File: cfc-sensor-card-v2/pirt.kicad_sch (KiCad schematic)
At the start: 82 parts, among them Q6 PMV45EN, Q7 DMP3050LVT-7, U1 TLC3704, U10 LT3042IMSE, U11 LT3042IMSE, U12 U-PIRT-PIRT1280A1-12, U13 XO_ISM95-XXXXXX, U6 LP2985-3.3, U7 LT3042IMSE, U8 LT3042IMSE, U9 LT3042IMSE

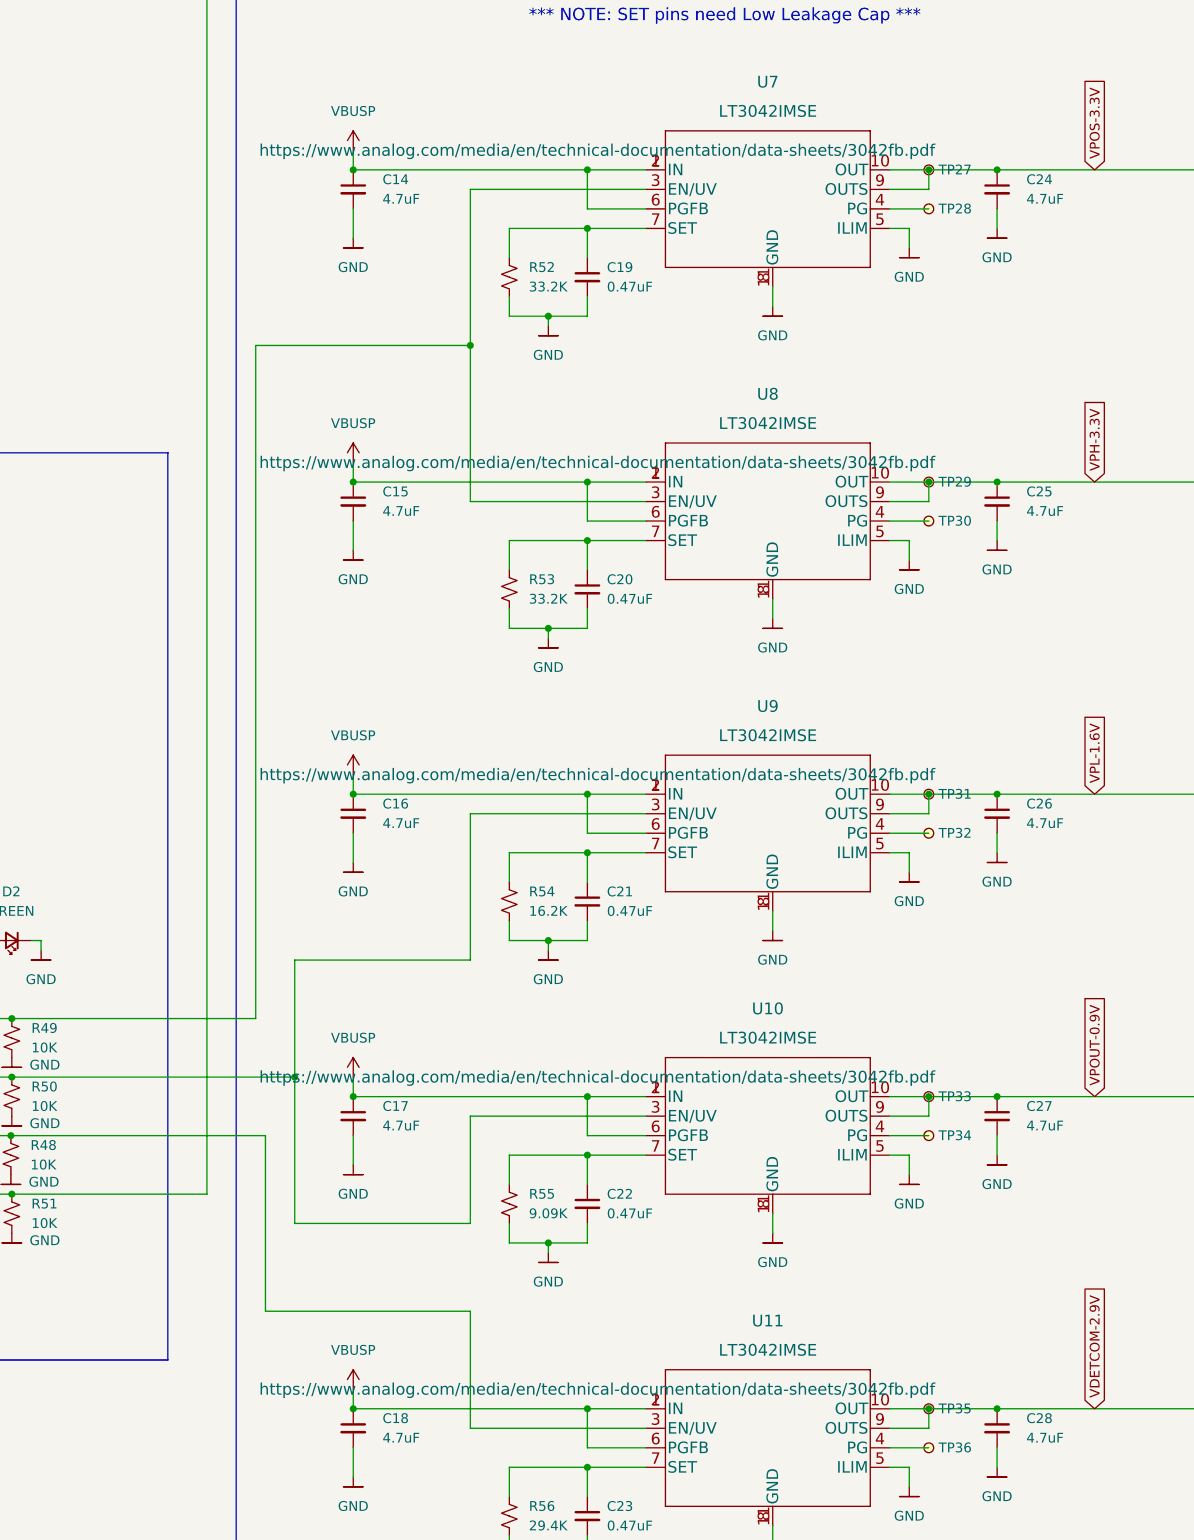
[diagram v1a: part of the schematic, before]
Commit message: OPD CB shunt resistor is 10m, not 100m. Cleanup documentation. Also clean up documentation on other pages.
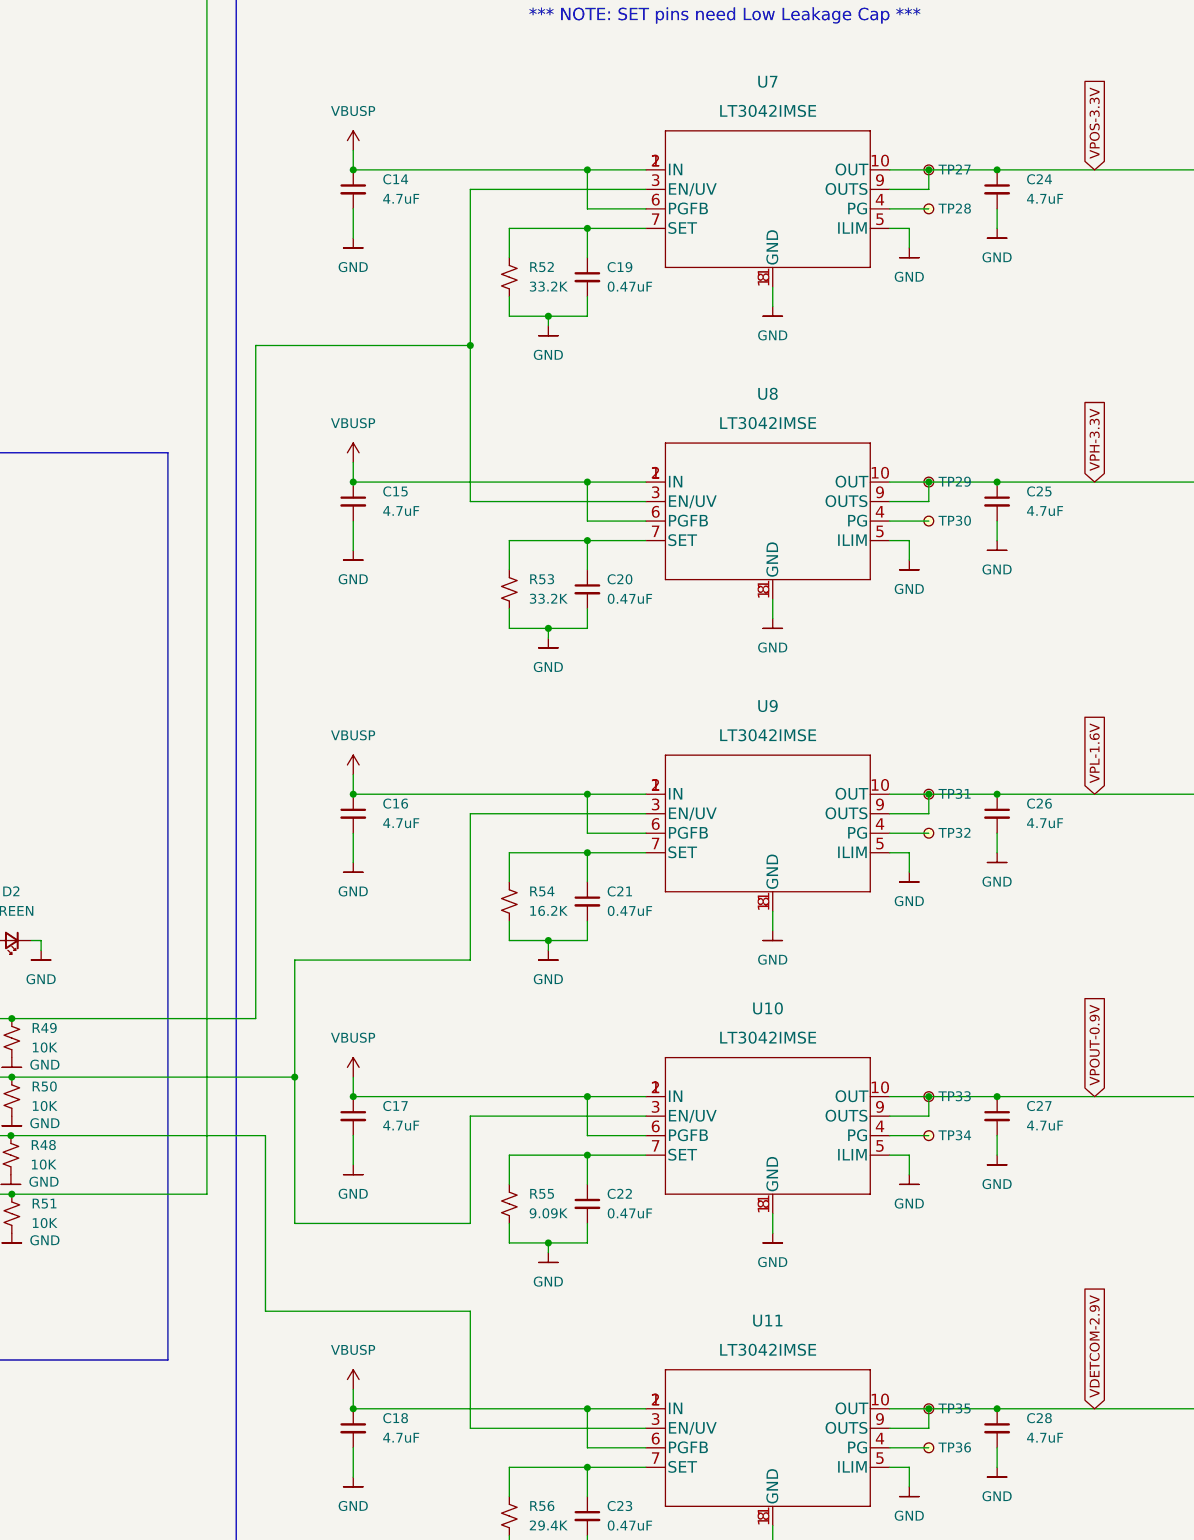
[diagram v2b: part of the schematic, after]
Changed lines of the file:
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@@
     )
     (property "Datasheet" "https://www.analog.com/media/en/technical-documentation/data-sheets/3042fb.pdf" (id 3) (at 193.04 224.79 0)
-      (effects (font (size 1.524 1.524)))
+      (effects (font (size 1.524 1.524)) hide)
     )
     (property "DIST" "Digikey" (id 4) (at 194.31 227.33 0)
@@
     )
     (property "Datasheet" "https://www.analog.com/media/en/technical-documentation/data-sheets/3042fb.pdf" (id 3) (at 193.04 104.14 0)
-      (effects (font (size 1.524 1.524)))
+      (effects (font (size 1.524 1.524)) hide)
     )
     (property "DIST" "Digikey" (id 4) (at 194.31 106.68 0)
@@
     )
     (property "Datasheet" "https://www.analog.com/media/en/technical-documentation/data-sheets/3042fb.pdf" (id 3) (at 193.04 184.15 0)
-      (effects (font (size 1.524 1.524)))
+      (effects (font (size 1.524 1.524)) hide)
     )
     (property "DIST" "Digikey" (id 4) (at 194.31 186.69 0)
@@
     )
     (property "Datasheet" "https://www.analog.com/media/en/technical-documentation/data-sheets/3042fb.pdf" (id 3) (at 193.04 144.78 0)
-      (effects (font (size 1.524 1.524)))
+      (effects (font (size 1.524 1.524)) hide)
     )
     (property "DIST" "Digikey" (id 4) (at 194.31 147.32 0)
@@
     )
     (property "Datasheet" "https://www.analog.com/media/en/technical-documentation/data-sheets/3042fb.pdf" (id 3) (at 193.04 63.5 0)
-      (effects (font (size 1.524 1.524)))
+      (effects (font (size 1.524 1.524)) hide)
     )
     (property "DIST" "Digikey" (id 4) (at 194.31 66.04 0)

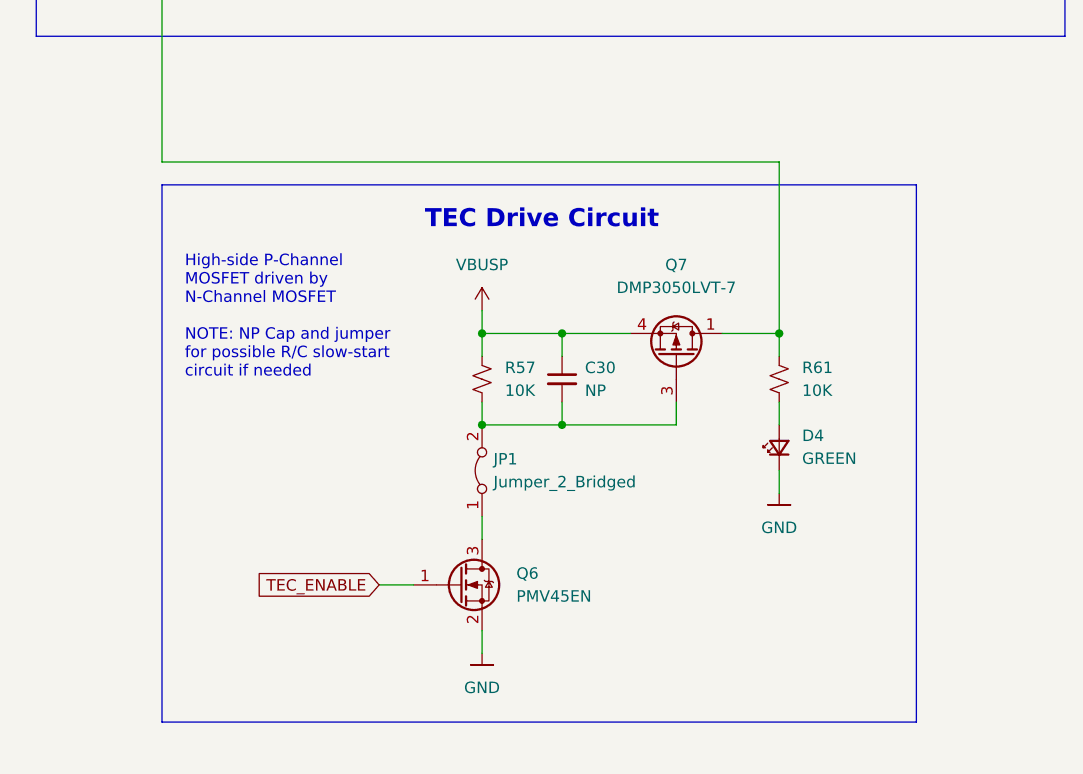
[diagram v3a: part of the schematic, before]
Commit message: Added soft start to sensor card and cleaned up some KiCad warnings
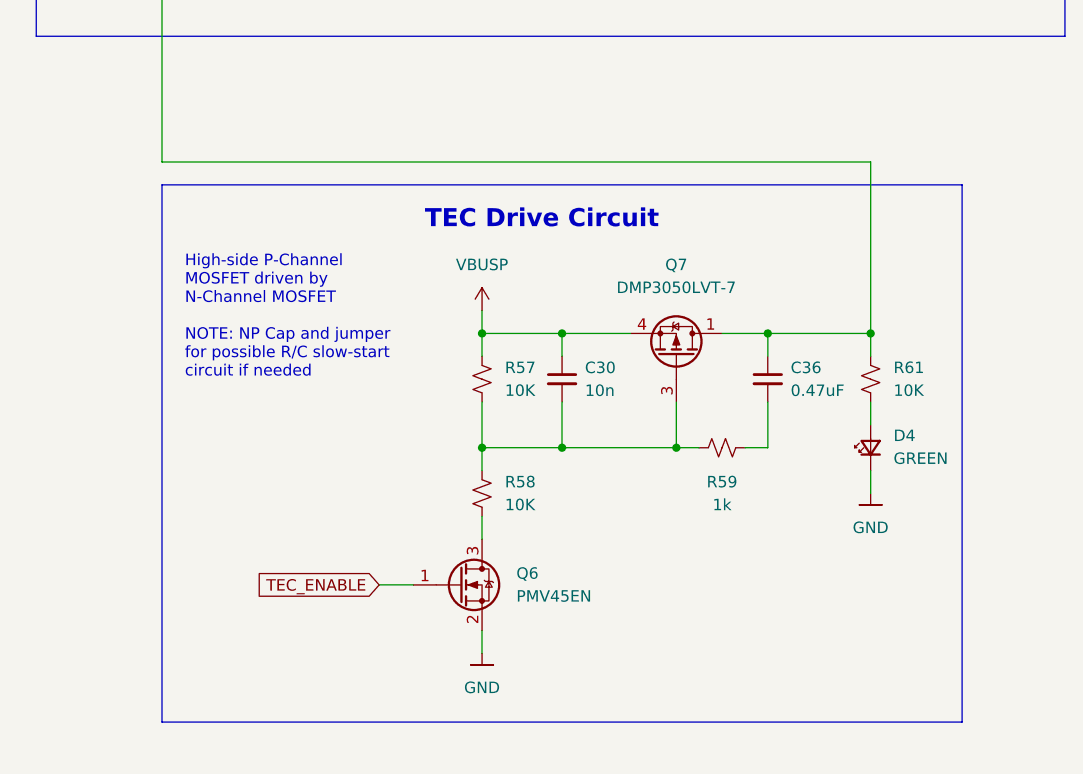
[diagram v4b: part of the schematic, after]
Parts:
- removed JP1: Jumper_2_Bridged, Jumper:SolderJumper-2_P1.3mm_Bridged_RoundedPad1.0x1.5mm, symbol Jumper:Jumper_2_Bridged
- added C36: 0.47uF, Capacitor_SMD:C_0603_1608Metric_Pad1.08x0.95mm_HandSolder, symbol Device:C_Small
- added R58: 10K, Resistor_SMD:R_0603_1608Metric_Pad0.98x0.95mm_HandSolder, symbol Device:R_Small_US
- added R59: 1k, Resistor_SMD:R_0603_1608Metric_Pad0.98x0.95mm_HandSolder, symbol Device:R_Small_US
- C30: value NP -> 10n
- TP16, TP17, TP20, TP23, TP24, TP25, TP26, TP27, TP28, TP29, TP30, TP31, TP32, TP33, TP34, TP35, TP36, TP37, TP38: footprint oresat-misc:TestPoint-MinTH -> oresat-misc:TestPoint-0.75mm-th
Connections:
- net at Q7.1 (D), Q7.2 (D), Q7.5 (D)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: now also C36.1
- net at C30.2, Q7.3 (G), R57.2: now also R58.1, R59.1
- net at Q6.3 (D): now also R58.2
- new net: C36.2, R59.2
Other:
- moved on the sheet: D4, R61

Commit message: Big sweep through to clean up from v2.0 to v2.1 board. Cleaned up all of the Github issues, and even added a MPS2410A CC driver to run the TEC for increased efficiency. Left old switch on board just in case. Lots of cleanup, added some documentation, added pin holes for 1.5 mm alignment pins, now version 2.1
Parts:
- removed C30: 10n, Capacitor_SMD:C_0603_1608Metric_Pad1.08x0.95mm_HandSolder, symbol Device:C_Small
- removed C36: 0.47uF, Capacitor_SMD:C_0603_1608Metric_Pad1.08x0.95mm_HandSolder, symbol Device:C_Small
- removed D4: GREEN, LED_SMD:LED_0603_1608Metric_Pad1.05x0.95mm_HandSolder, symbol Device:LED_Small
- removed Q6: PMV45EN, Package_TO_SOT_SMD:SOT-23-3, symbol Device:Q_NMOS_GSD
- removed Q7: DMP3050LVT-7, Package_TO_SOT_SMD:SOT-23-6_Handsoldering, symbol oresat-transistors:DMP3050LVT-7
- removed R57, R58, R61: 10K, Resistor_SMD:R_0603_1608Metric_Pad0.98x0.95mm_HandSolder, symbol Device:R_Small_US
- removed R59: 1k, Resistor_SMD:R_0603_1608Metric_Pad0.98x0.95mm_HandSolder, symbol Device:R_Small_US
- D2: footprint LED_SMD:LED_0603_1608Metric_Pad1.05x0.95mm_HandSolder -> LED_SMD:LED_0603_1608Metric
- U1: DIST Digikey -> (none); DPN 296-39242-1-ND -> (none); MFR Texas Instruments -> (none); MPN TLC3704IPWR -> (none)
- U10, U11, U7, U8, U9: footprint Package_SO:MSOP-10-1EP_3x3mm_P0.5mm_EP1.68x1.88mm_ThermalVias -> oresat-ics:MSOP-10-1EP_3x3mm_P0.5mm_EP1.68x1.88mm_0.254_ThermalVias
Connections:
- net GND: no longer U12.22 (TEC-)
- net TEC+: now reaches U12.23 (TEC+)
- new net: U12.2, U12.28, U12.3, U12.32, U12.33, U12.34, U12.35, U12.36, U12.37, U12.38, U12.39, U12.4, U12.40, U12.41, U12.42, U12.43
- new net TEC-: U12.22 (TEC-)
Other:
- note removed: "TEC Drive Circuit"
- note removed: "﻿High-side P-Channel MOSFET driven by N-Channel MOSFET ﻿NOTE: NP Cap and jumper for possible R/C slow-start circuit if needed"
- company: (none) -> Portland State Aerospace Society
- title: (none) -> CFC Sensor Card
